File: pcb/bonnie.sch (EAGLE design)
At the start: 9 parts

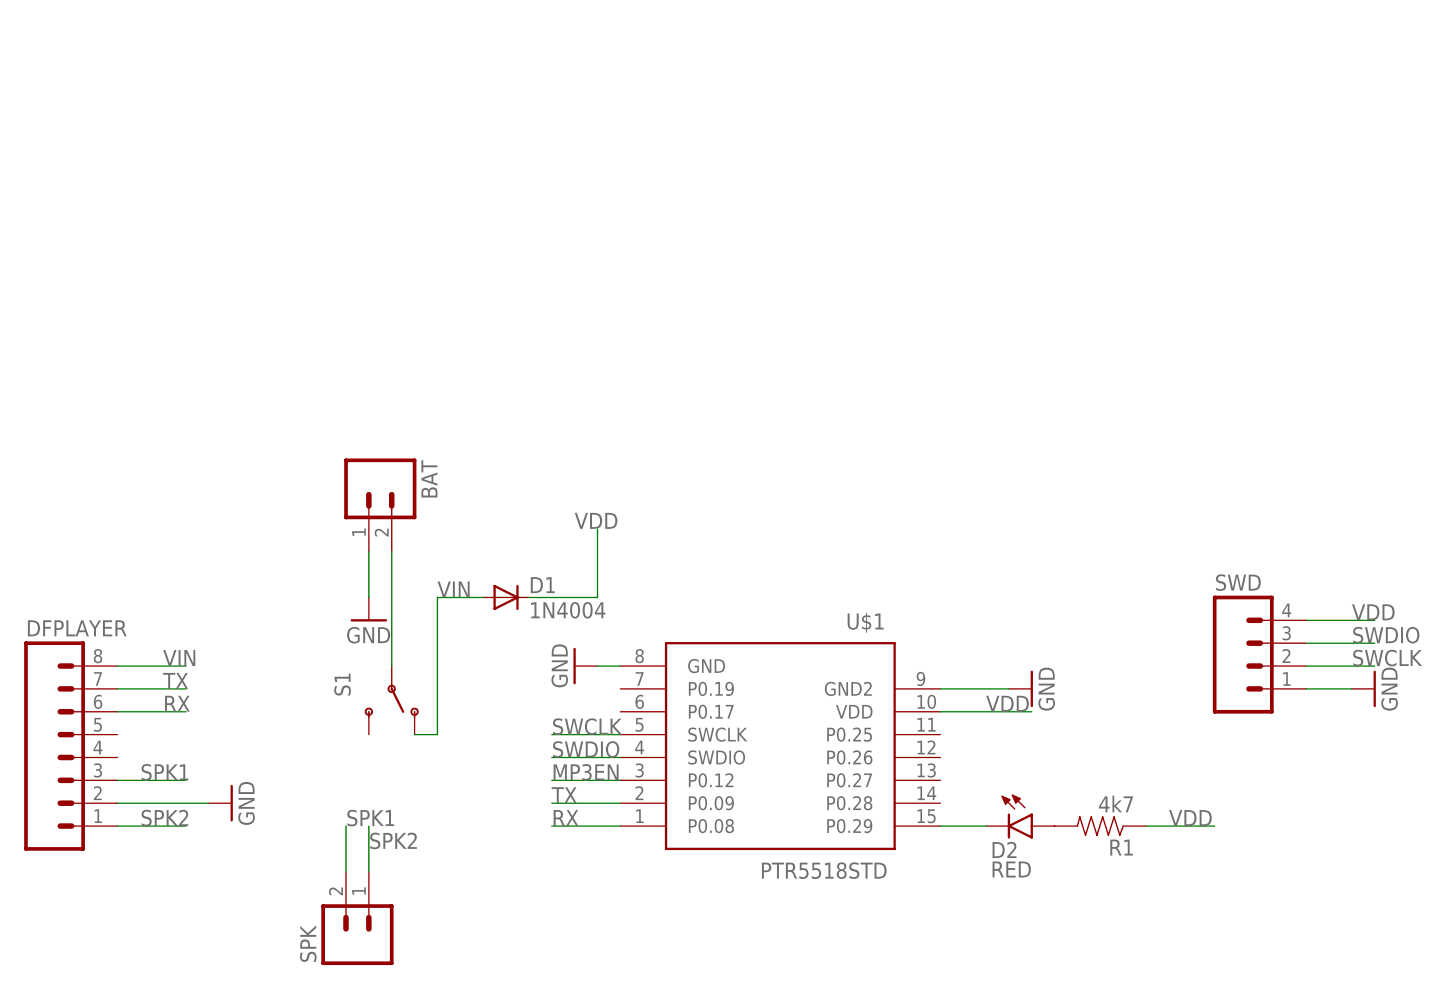
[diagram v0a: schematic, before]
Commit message: add charging mechanism, replace diode with a regulator
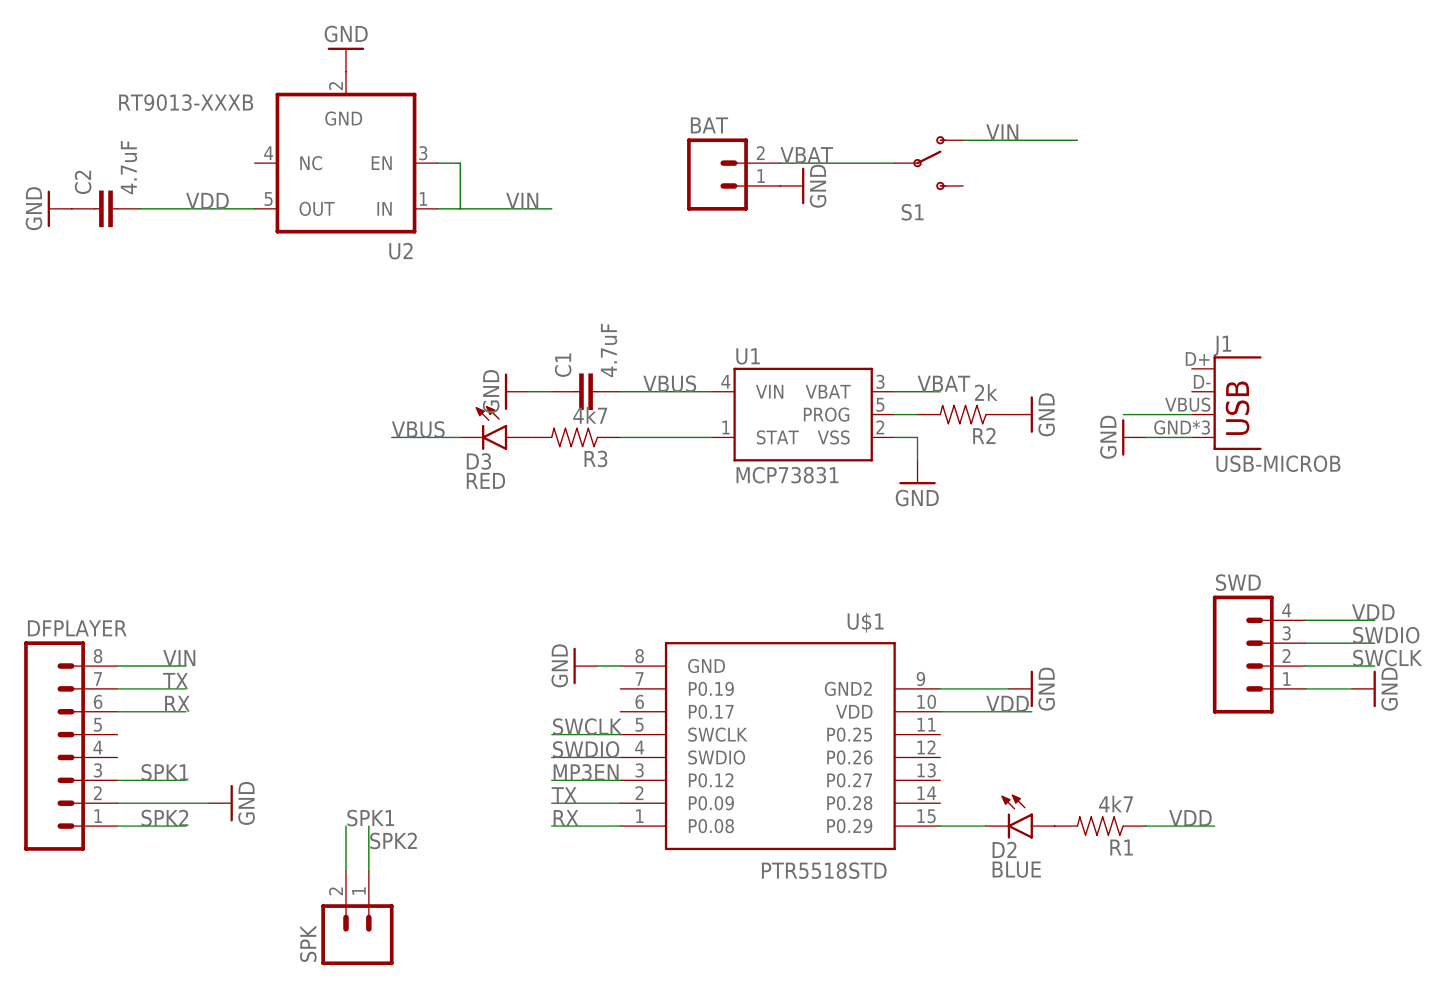
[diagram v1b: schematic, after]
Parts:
- removed D1: 1N4004, diode:1N4004
- added C1, C2: 4.7uF, SparkFun-Passives:CAP0603-CAP
- added D3: RED, SparkFun-LED:LED-RED1206
- added J1: USB-MICROB, SparkFun-Connectors:USB-MICROB
- added R2: 2k, SparkFun-Resistors:4.7OHM-1/10W-5%(0603)
- added R3: 4k7, SparkFun-Resistors:4.7OHM-1/10W-5%(0603)
- added U1: MCP73831, SparkFun-PowerIC:MCP73831
- added U2: RT9013-XXXB, v-reg-new:RT9013-XXXB
- D2: value RED -> BLUE
- SPK: device SparkFun-Connectors:M02JST-PTH-2 -> SparkFun-Connectors:M02JST-PTH-VERT
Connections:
- new net N$4: R3.1, U1.STAT
- new net N$5: D3.A, R3.2
- new net VBAT: BAT.2, S1.P, U1.VBAT
- new net VBUS: C1.2, D3.C, J1.VBUS, U1.VIN
- net GND: now also C1.1, C2.1, J1.GND, R2.1, U1.VSS, U2.GND
- net N$1: now also R2.2, U1.PROG; no longer BAT.2, S1.P
- net VDD: now also U2.OUT; no longer D1.C
- net VIN: now also U2.EN, U2.IN; no longer D1.A
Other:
- moved on the sheet: BAT, S1

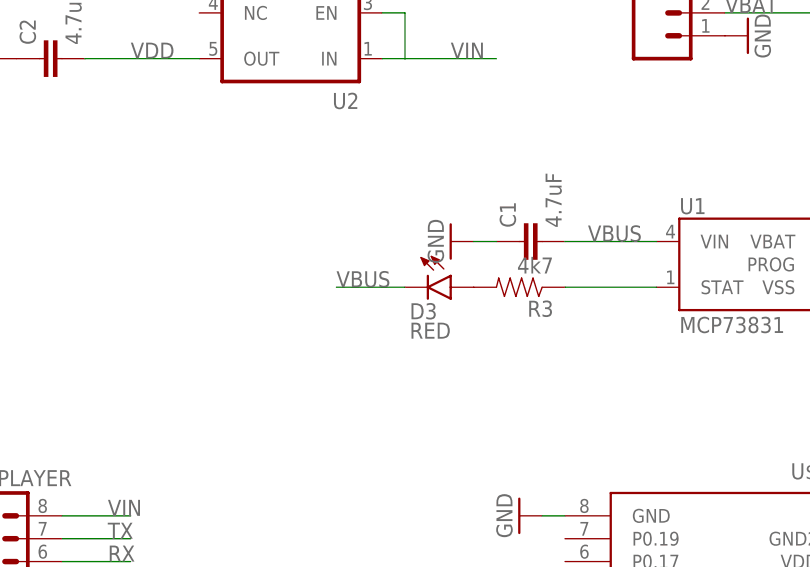
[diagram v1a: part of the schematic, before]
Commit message: fix: incorrect led oritentation
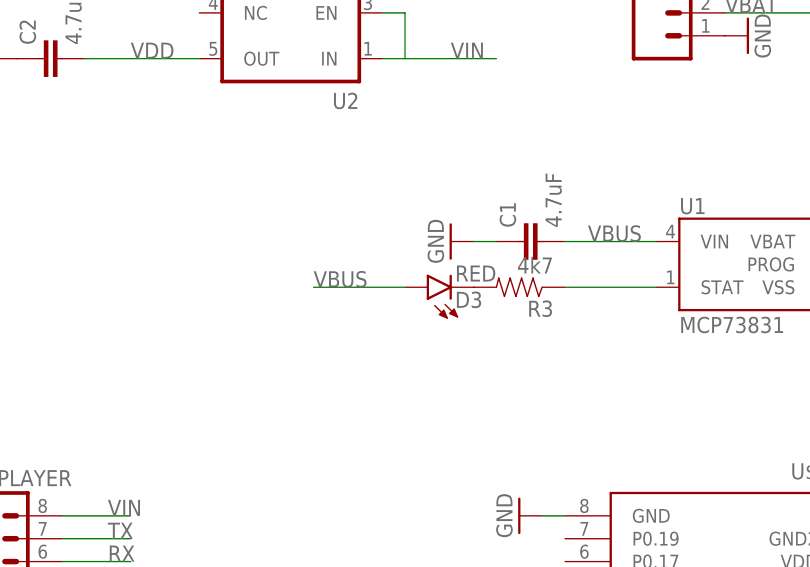
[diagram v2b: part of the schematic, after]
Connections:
- net N$5: now also D3.C; no longer D3.A
- net VBUS: now also D3.A; no longer D3.C
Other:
- moved on the sheet: D3
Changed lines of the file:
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@@
 <instance part="GND6" gate="1" x="91.44" y="83.82" rot="R270"/>
 <instance part="C1" gate="G$1" x="33.02" y="88.9" rot="R90"/>
-<instance part="GND7" gate="1" x="22.86" y="88.9" rot="R270"/>
+<instance part="GND7" gate="1" x="22.86" y="88.9" smashed="yes" rot="R270">
+<attribute name="VALUE" x="20.32" y="91.44" size="1.778" layer="96" rot="R270"/>
+</instance>
 <instance part="C2" gate="G$1" x="-20.32" y="109.22" rot="R90"/>
 <instance part="GND8" gate="1" x="-27.94" y="109.22" rot="R270"/>
@@
 <instance part="GND10" gate="1" x="68.58" y="78.74"/>
 <instance part="R3" gate="G$1" x="30.48" y="83.82" rot="R180"/>
-<instance part="D3" gate="G$1" x="22.86" y="83.82" rot="R270"/>
+<instance part="D3" gate="G$1" x="20.32" y="83.82" smashed="yes" rot="R90">
+<attribute name="NAME" x="26.416" y="83.312" size="1.778" layer="95" rot="R180"/>
+<attribute name="VALUE" x="27.94" y="86.233" size="1.778" layer="96" rot="R180"/>
+</instance>
 <instance part="U2" gate="G$1" x="5.08" y="114.3" rot="R180"/>
 <instance part="GND11" gate="1" x="5.08" y="127" rot="R180"/>
@@
 </segment>
 <segment>
-<pinref part="D3" gate="G$1" pin="C"/>
-<wire x1="17.78" y1="83.82" x2="10.16" y2="83.82" width="0.1524" layer="91"/>
-<label x="10.16" y="83.82" size="1.778" layer="95"/>
+<pinref part="D3" gate="G$1" pin="A"/>
+<wire x1="17.78" y1="83.82" x2="7.62" y2="83.82" width="0.1524" layer="91"/>
+<label x="7.62" y="83.82" size="1.778" layer="95"/>
 </segment>
 </net>
@@
 <segment>
 <pinref part="R3" gate="G$1" pin="2"/>
-<pinref part="D3" gate="G$1" pin="A"/>
-</segment>
-</net>
+<pinref part="D3" gate="G$1" pin="C"/>
+</segment>
+</net>

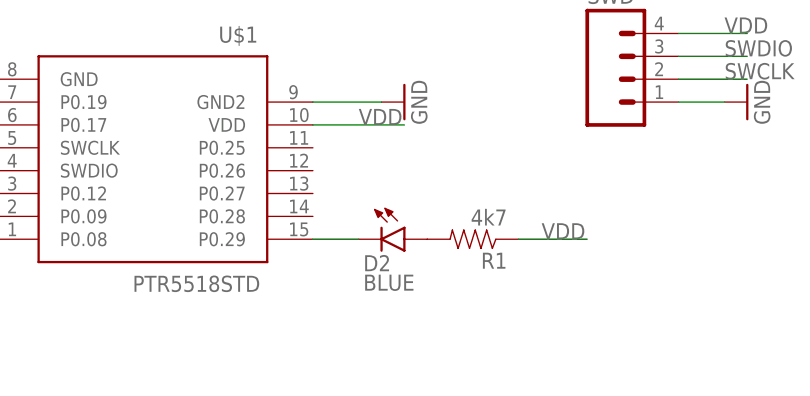
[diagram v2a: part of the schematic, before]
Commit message: switch to smaller package for LEDs (1206 -> 0603)
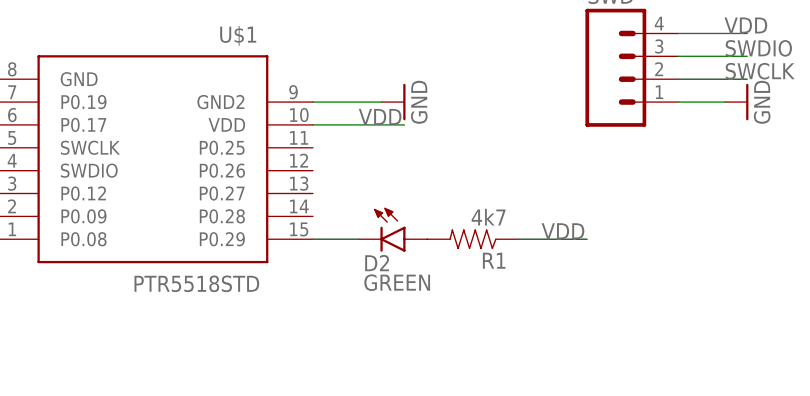
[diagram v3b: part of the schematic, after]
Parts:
- D2: value BLUE -> GREEN; device SparkFun-LED:LED-RED1206 -> SparkFun-LED:LED-GREEN0603
- D3: device SparkFun-LED:LED-RED1206 -> SparkFun-LED:LED-RED0603
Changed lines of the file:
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@@
 <part name="GND5" library="SparkFun-Aesthetics" deviceset="GND" device=""/>
 <part name="SPK" library="SparkFun-Connectors" deviceset="M02" device="JST-PTH-VERT"/>
-<part name="D2" library="SparkFun-LED" deviceset="LED-RED" device="1206" value="BLUE"/>
+<part name="D2" library="SparkFun-LED" deviceset="LED-GREEN" device="0603" value="GREEN"/>
 <part name="R1" library="SparkFun-Resistors" deviceset="4.7OHM-1/10W-5%(0603)" device="" value="4k7"/>
 <part name="U1" library="SparkFun-PowerIC" deviceset="MCP73831" device=""/>
@@
 <part name="GND10" library="SparkFun-Aesthetics" deviceset="GND" device=""/>
 <part name="R3" library="SparkFun-Resistors" deviceset="4.7OHM-1/10W-5%(0603)" device="" value="4k7"/>
-<part name="D3" library="SparkFun-LED" deviceset="LED-RED" device="1206" value="RED"/>
+<part name="D3" library="SparkFun-LED" deviceset="LED-RED" device="0603" value="RED"/>
 <part name="U2" library="v-reg-new" deviceset="RT9013-XXX" device="B"/>
 <part name="GND11" library="SparkFun-Aesthetics" deviceset="GND" device=""/>

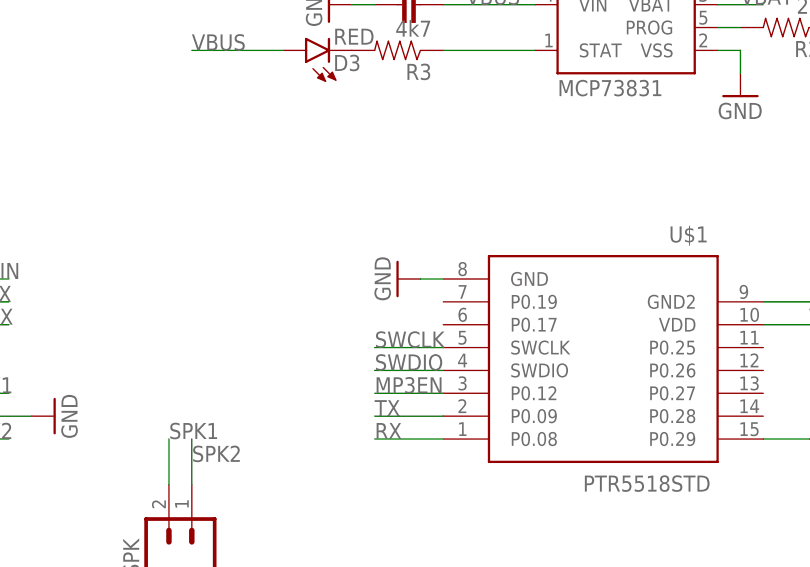
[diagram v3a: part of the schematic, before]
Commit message: update board for PTR5618 module
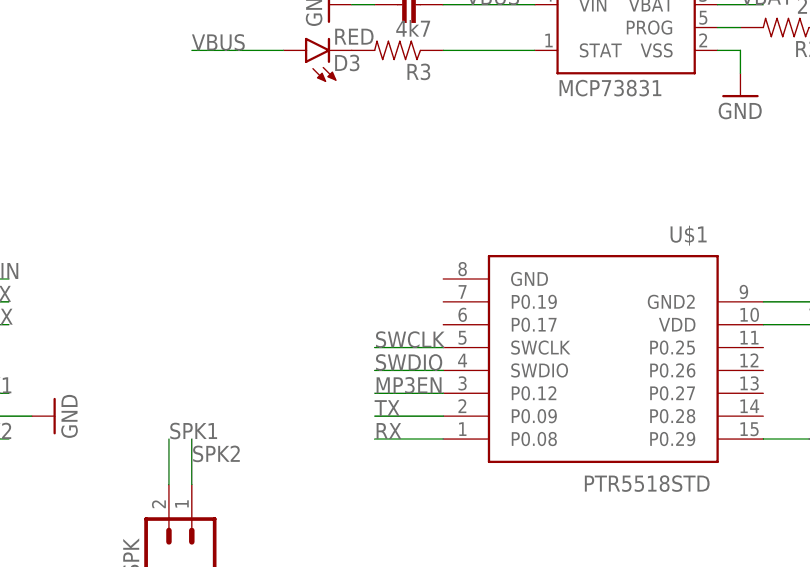
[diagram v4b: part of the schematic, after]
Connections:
- net GND: no longer U$1.GND
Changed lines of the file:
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@@
 <part name="U$1" library="PTR5518" deviceset="PTR5518" device="STD"/>
 <part name="SWD" library="SparkFun-Connectors" deviceset="M04" device="LOCK"/>
-<part name="GND1" library="SparkFun-Aesthetics" deviceset="GND" device=""/>
 <part name="GND2" library="SparkFun-Aesthetics" deviceset="GND" device=""/>
 <part name="GND3" library="SparkFun-Aesthetics" deviceset="GND" device=""/>
@@
 <instance part="U$1" gate="G$1" x="53.34" y="48.26" rot="MR0"/>
 <instance part="SWD" gate="G$1" x="106.68" y="58.42"/>
-<instance part="GND1" gate="1" x="30.48" y="58.42" rot="R270"/>
 <instance part="GND2" gate="1" x="81.28" y="55.88" rot="R90"/>
 <instance part="GND3" gate="1" x="119.38" y="55.88" rot="R90"/>
@@
 <net name="GND" class="0">
 <segment>
-<pinref part="GND1" gate="1" pin="GND"/>
-<pinref part="U$1" gate="G$1" pin="GND"/>
-<wire x1="33.02" y1="58.42" x2="35.56" y2="58.42" width="0.1524" layer="91"/>
-</segment>
-<segment>
 <pinref part="GND3" gate="1" pin="GND"/>
